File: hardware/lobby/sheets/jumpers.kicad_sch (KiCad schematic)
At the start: 8 parts, among them SW1 SW_SPST, SW2 SW_SPST

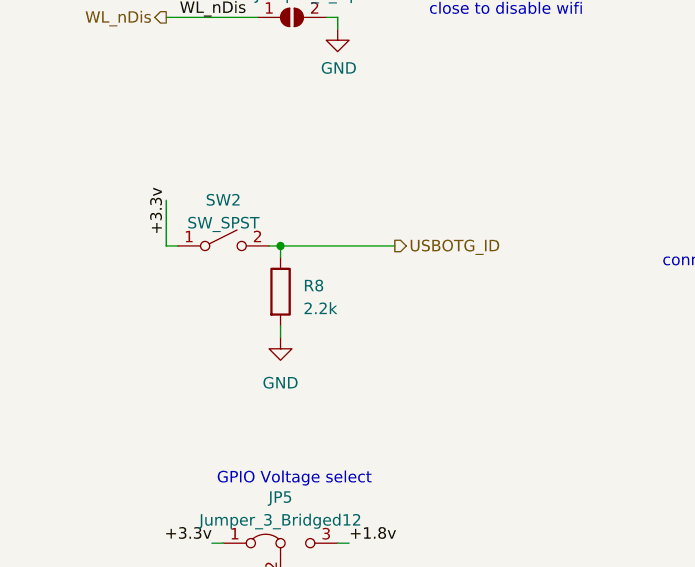
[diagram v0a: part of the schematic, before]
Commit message: change fusb42mx to qfn package
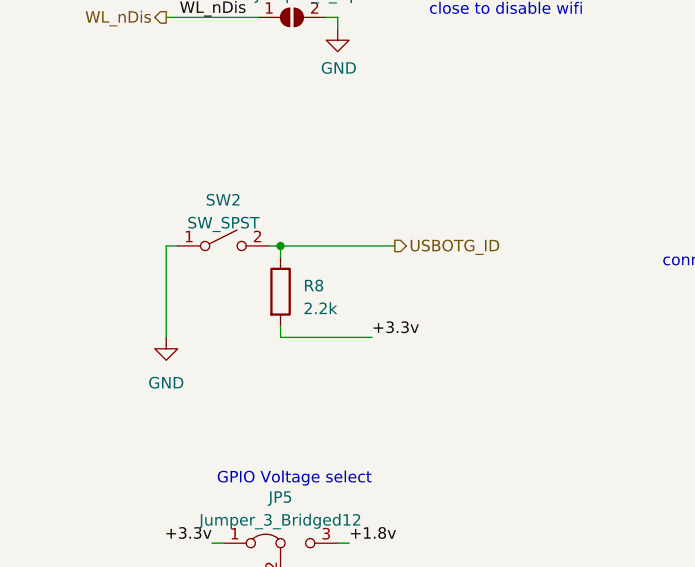
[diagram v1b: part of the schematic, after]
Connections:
- net +3.3v: now also R8.2; no longer SW2.1 (A)
- net GND: now also SW2.1 (A); no longer R8.2
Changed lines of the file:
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@@
     (stroke (width 0) (type solid) (color 0 0 0 0))
   )
-  (wire (pts (xy 26.67 118.11) (xy 26.67 123.19))
+  (wire (pts (xy 26.67 123.19) (xy 26.67 133.35))
     (stroke (width 0) (type solid) (color 0 0 0 0))
   )
@@
   )
   (wire (pts (xy 39.37 132.08) (xy 39.37 133.35))
+    (stroke (width 0) (type solid) (color 0 0 0 0))
+  )
+  (wire (pts (xy 39.37 133.35) (xy 49.53 133.35))
     (stroke (width 0) (type solid) (color 0 0 0 0))
   )
@@
     (effects (font (size 1.27 1.27)) (justify right bottom))
   )
-  (label "+3.3v" (at 26.67 121.92 90)
-    (effects (font (size 1.27 1.27)) (justify left bottom))
-  )
   (label "+3.3v" (at 31.75 156.21 180)
     (effects (font (size 1.27 1.27)) (justify right bottom))
@@
   )
   (label "+1.8v" (at 46.99 156.21 0)
+    (effects (font (size 1.27 1.27)) (justify left bottom))
+  )
+  (label "+3.3v" (at 49.53 133.35 0)
     (effects (font (size 1.27 1.27)) (justify left bottom))
   )
@@
     (effects (font (size 1.27 1.27)) (justify left))
   )
-  (symbol (lib_id "power:GND") (at 39.37 133.35 0) (unit 1)
+  (symbol (lib_id "power:GND") (at 26.67 133.35 0) (unit 1)
     (in_bom yes) (on_board yes) (fields_autoplaced)
-    (property "Reference" "#PWR061" (id 0) (at 39.37 139.7 0)
+    (property "Reference" "#PWR061" (id 0) (at 26.67 139.7 0)
       (effects (font (size 1.27 1.27)) hide)
     )
-    (property "Value" "GND" (id 1) (at 39.37 138.43 0))
-    (property "Footprint" "" (id 2) (at 39.37 133.35 0)
+    (property "Value" "GND" (id 1) (at 26.67 138.43 0))
+    (property "Footprint" "" (id 2) (at 26.67 133.35 0)
       (effects (font (size 1.27 1.27)) hide)
     )
-    (property "Datasheet" "" (id 3) (at 39.37 133.35 0)
+    (property "Datasheet" "" (id 3) (at 26.67 133.35 0)
       (effects (font (size 1.27 1.27)) hide)
     )
